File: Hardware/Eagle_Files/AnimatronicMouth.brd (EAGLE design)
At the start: 82.2 x 82.5 mm, 50 parts, among them IC1 QUAD_OPAMPP, IC2 74HCT125N, J1 USB_B_PTH, J2 AUDIO_JACK_3.5MM_KIT

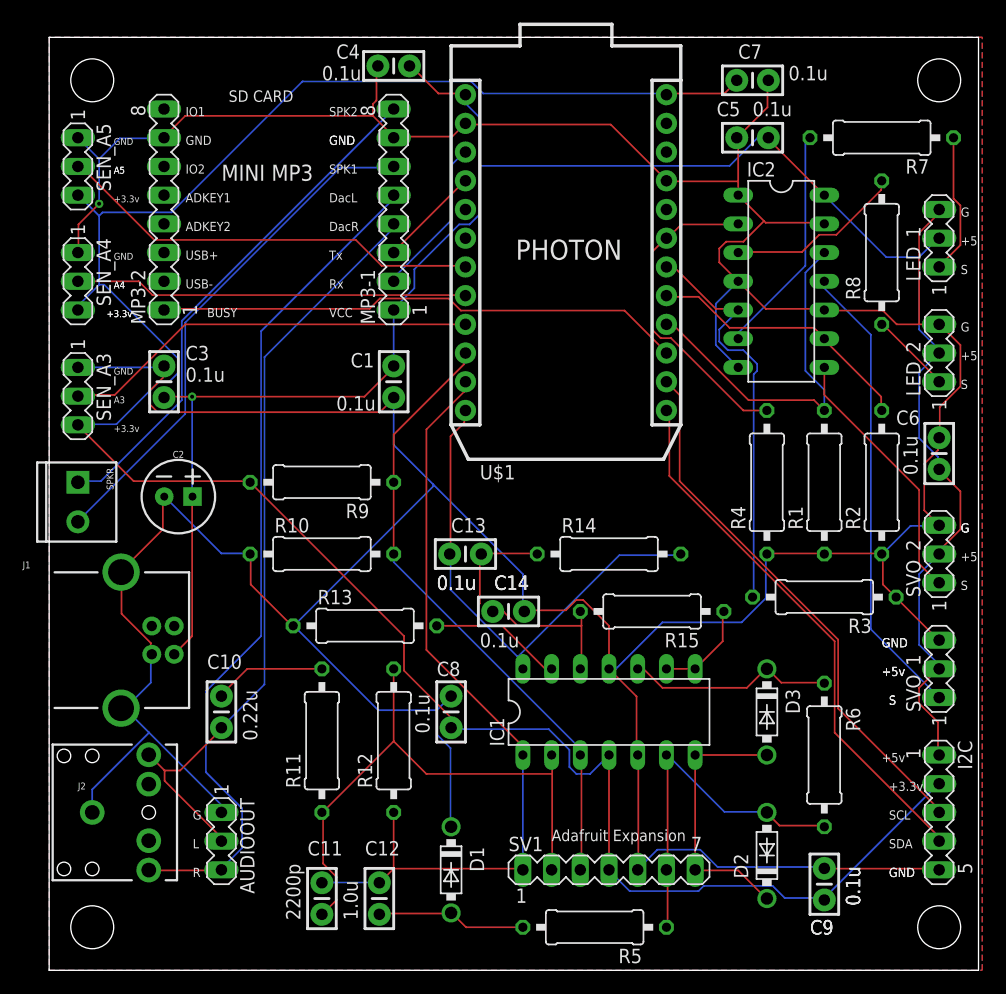
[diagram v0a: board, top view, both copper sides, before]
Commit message: Posted correct eagle files
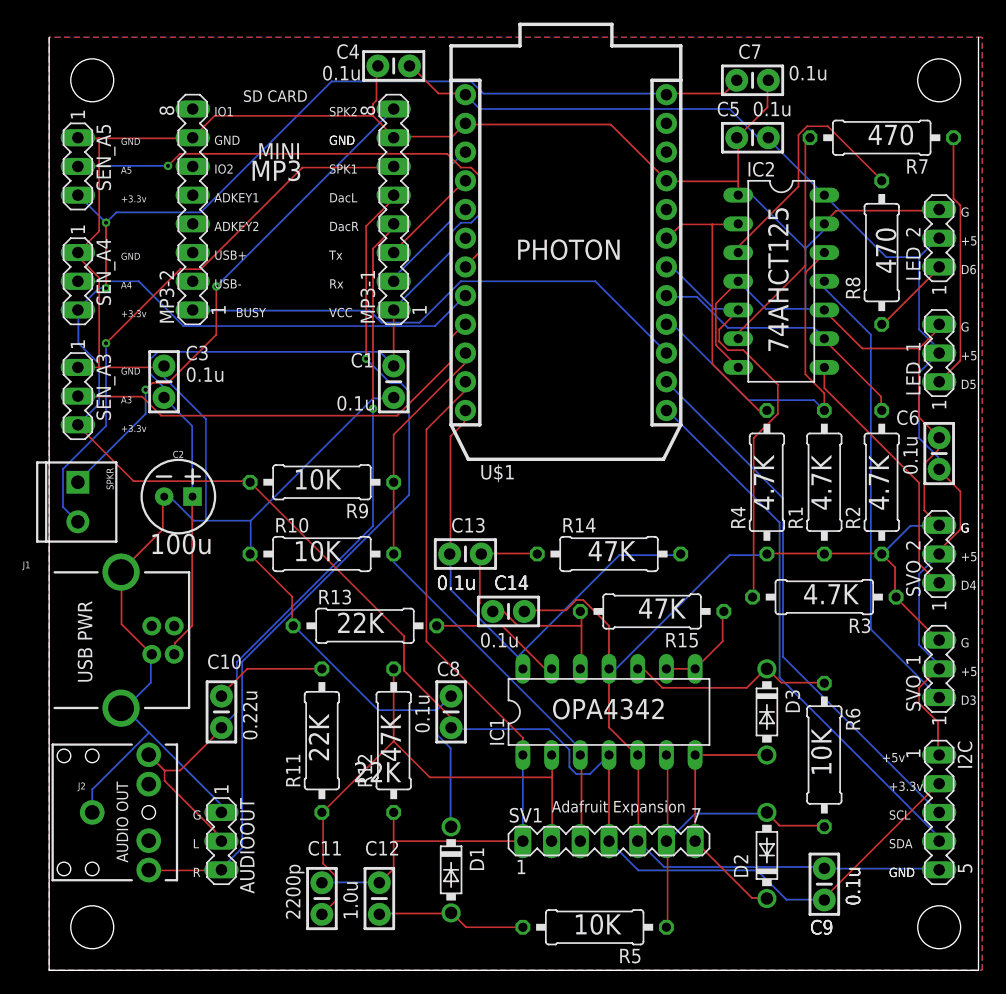
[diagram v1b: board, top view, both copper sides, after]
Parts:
- moved LED_1 10.2 mm to (78.7, 54.6)
- moved LED_2 10.2 mm to (78.7, 64.8)
- moved MP3-2 2.54 mm to (12.7, 67.3)
- moved SV1 2.54 mm to (49.5, 11.4)
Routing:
- net GND: track 439.8 -> 410.1 mm, vias 1 -> 0
- net VCCA: track 204.8 -> 193.4 mm, vias 0 -> 2
- net N$8: track 12.5 -> 22.6 mm
- net N$28: track 38.0 -> 45.4 mm, vias 0 -> 1
- net N$11: track 15.8 -> 22.3 mm
- net VCC: track 177.2 -> 182.9 mm, vias 1 -> 0
- net N$12: track 45.8 -> 49.9 mm, vias 0 -> 1
- net N$4: track 28.7 -> 25.8 mm
- net N$30: track 36.9 -> 39.6 mm
- net N$13: track 71.5 -> 68.9 mm
- net N$14: track 55.4 -> 52.9 mm
- net N$21: track 50.9 -> 48.5 mm
- net N$31: track 34.8 -> 37.0 mm
- net N$18: track 23.9 -> 22.4 mm
- net N$2: track 36.5 -> 38.0 mm
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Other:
- board text added: "(c) 2021, TEAM PRACTICAL PROJECTS"
- board text added: "100u"
- board text added: "10K"
- board text added: "22K"
- board text added: "4.7K"
- board text added: "470"
- board text added: "47K"
- board text added: "74AHCT125"
- board text added: "ANIMATRONICS PROJECT"
- board text added: "AUDIO OUT"
- board text added: "All Rights Reserved"
- board text added: "D3"
- board text added: "D4"
- board text added: "D5"
- board text added: "D6"
- board text added: "MINI"
- board text added: "MOUTH DRIVER BOARD"
- board text added: "MP3"
- board text added: "OPA4342"
- board text added: "USB PWR"
- board text removed: "MINI MP3"
- board text removed: "S"

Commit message: Updated Eagle Files
Corrected Board Outline problem.  This design is released for production.
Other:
- board size 82.2 x 82.5 mm -> 82.5 x 82.5 mm
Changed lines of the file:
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@@
 <setting verticaltext="up"/>
 </settings>
-<grid distance="0.025" unitdist="inch" unit="inch" style="lines" multiple="1" display="yes" altdistance="5" altunitdist="mil" altunit="mil"/>
+<grid distance="0.05" unitdist="inch" unit="inch" style="lines" multiple="1" display="yes" altdistance="5" altunitdist="mil" altunit="mil"/>
 <layers>
 <layer number="1" name="Top" color="4" fill="1" visible="yes" active="yes"/>
@@
 </polygon>
 <text x="17.78" y="69.85" size="1.778" layer="21">MP3</text>
+<wire x1="82.22" y1="0" x2="82.55" y2="0" width="0" layer="20"/>
+<wire x1="82.55" y1="0" x2="82.55" y2="82.55" width="0" layer="20"/>
+<wire x1="82.55" y1="82.55" x2="0" y2="82.55" width="0" layer="20"/>
+<wire x1="0" y1="82.55" x2="0" y2="82.54" width="0" layer="20"/>
 </plain>
 <attributes>
